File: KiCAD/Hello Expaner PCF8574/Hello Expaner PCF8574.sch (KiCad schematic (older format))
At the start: 27 parts

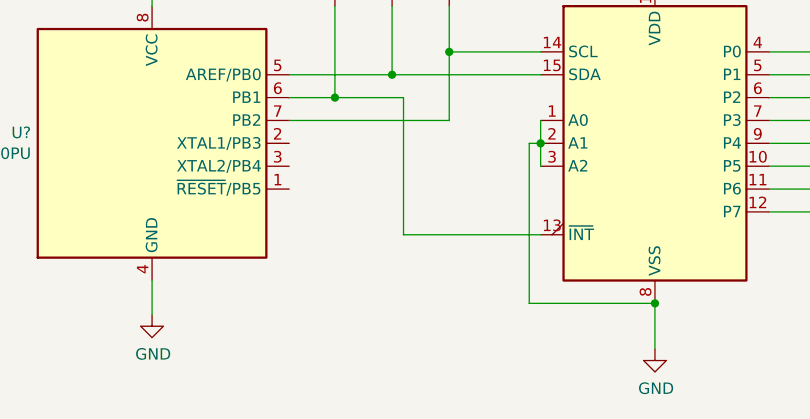
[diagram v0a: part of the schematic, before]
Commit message: Added assembler file for Expander project
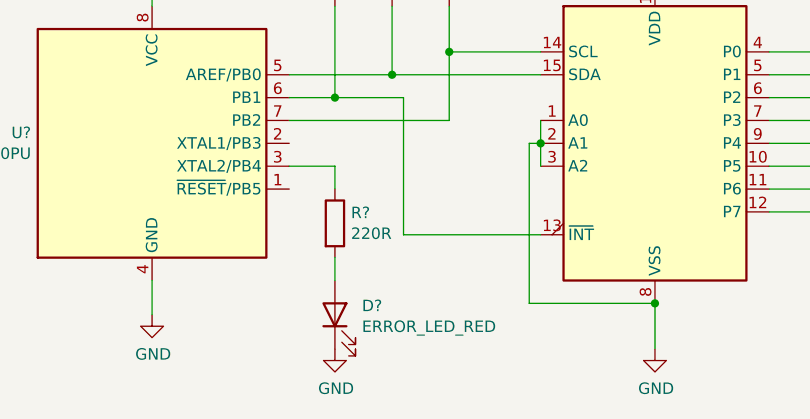
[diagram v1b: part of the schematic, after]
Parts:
- added D?: ERROR_LED_RED, symbol Device:LED
- added R?: 220R, symbol Device:R
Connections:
- net GND: now also D?.1 (K)
- net at U?.3 (XTAL2/PB4): now also R?.1
- new net: D?.2 (A), R?.2
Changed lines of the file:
@@
 Comp ""
 Comment1 ""
-Comment2 "All LEDs are green"
+Comment2 "All LEDs (except one PB4) are green and active when state on pin is LOW"
 Comment3 "P4 - P7 are configured as inputs"
 Comment4 "P0 - P3 are configured as outputs"
@@
 	1    0    0    -1
 $EndComp
+$Comp
+L Device:LED D?
+U 1 1 60EB9EA7
+P 2450 4800
+F 0 "D?" V 2489 4682 50  0000 R CNN
+F 1 "ERROR_LED_RED" V 2398 4682 50  0000 R CNN
+F 2 "" H 2450 4800 50  0001 C CNN
+F 3 "~" H 2450 4800 50  0001 C CNN
+	1    2450 4800
+	0    -1   -1   0
+$EndComp
+$Comp
+L Device:R R?
+U 1 1 60EB9EAD
+P 2450 4400
+F 0 "R?" H 2520 4446 50  0000 L CNN
+F 1 "220R" H 2520 4355 50  0000 L CNN
+F 2 "" V 2380 4400 50  0001 C CNN
+F 3 "~" H 2450 4400 50  0001 C CNN
+	1    2450 4400
+	1    0    0    -1
+$EndComp
+Wire Wire Line
+	2450 4550 2450 4650
+Wire Wire Line
+	2250 4150 2450 4150
+Wire Wire Line
+	2450 4150 2450 4250
+$Comp
+L power:GND #PWR?
+U 1 1 60EBDD1B
+P 2450 4950
+F 0 "#PWR?" H 2450 4700 50  0001 C CNN
+F 1 "GND" H 2455 4777 50  0000 C CNN
+F 2 "" H 2450 4950 50  0001 C CNN
+F 3 "" H 2450 4950 50  0001 C CNN
+	1    2450 4950
+	1    0    0    -1
+$EndComp
